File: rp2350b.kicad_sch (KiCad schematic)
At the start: 34 parts, among them J6 SM03B-SRSS-TB, SW1 SW_Push, SW2 SW_Push, U10 W25Q128JVS, U13 RP2350_80QFN, Y2 ABM8-272-T3

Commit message: Break out RP2350
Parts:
- SW1, SW2: footprint Button_Switch_SMD:SW_Push_1P1T_NO_Vertical_Wuerth_434133025816 -> Button_Switch_SMD:SW_Push_1P1T_XKB_TS-1187A; LCSC (none) -> C318884
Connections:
- net +1V1: now also C20.1, C22.1, C23.1, U13.10 (DVDD), U13.32 (DVDD), U13.51 (DVDD)
- net SWCLK: no longer U13.33 (SWCLK)
- net SWD: no longer U13.34 (SWD)
- net GPIO0 renamed GPIO00
- net GPIO1 renamed GPIO01
- net GPIO2 renamed GPIO02
- net GPIO3 renamed GPIO03
- net GPIO4 renamed GPIO04
- net GPIO5 renamed GPIO05
- net GPIO6 renamed GPIO06
- net GPIO7 renamed GPIO07
- net GPIO8 renamed GPIO08
- net GPIO9 renamed GPIO09
- new net SWD.SWCLK: U13.33 (SWCLK)
- new net SWD.SWD: U13.34 (SWD)
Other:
- moved on the sheet: J6

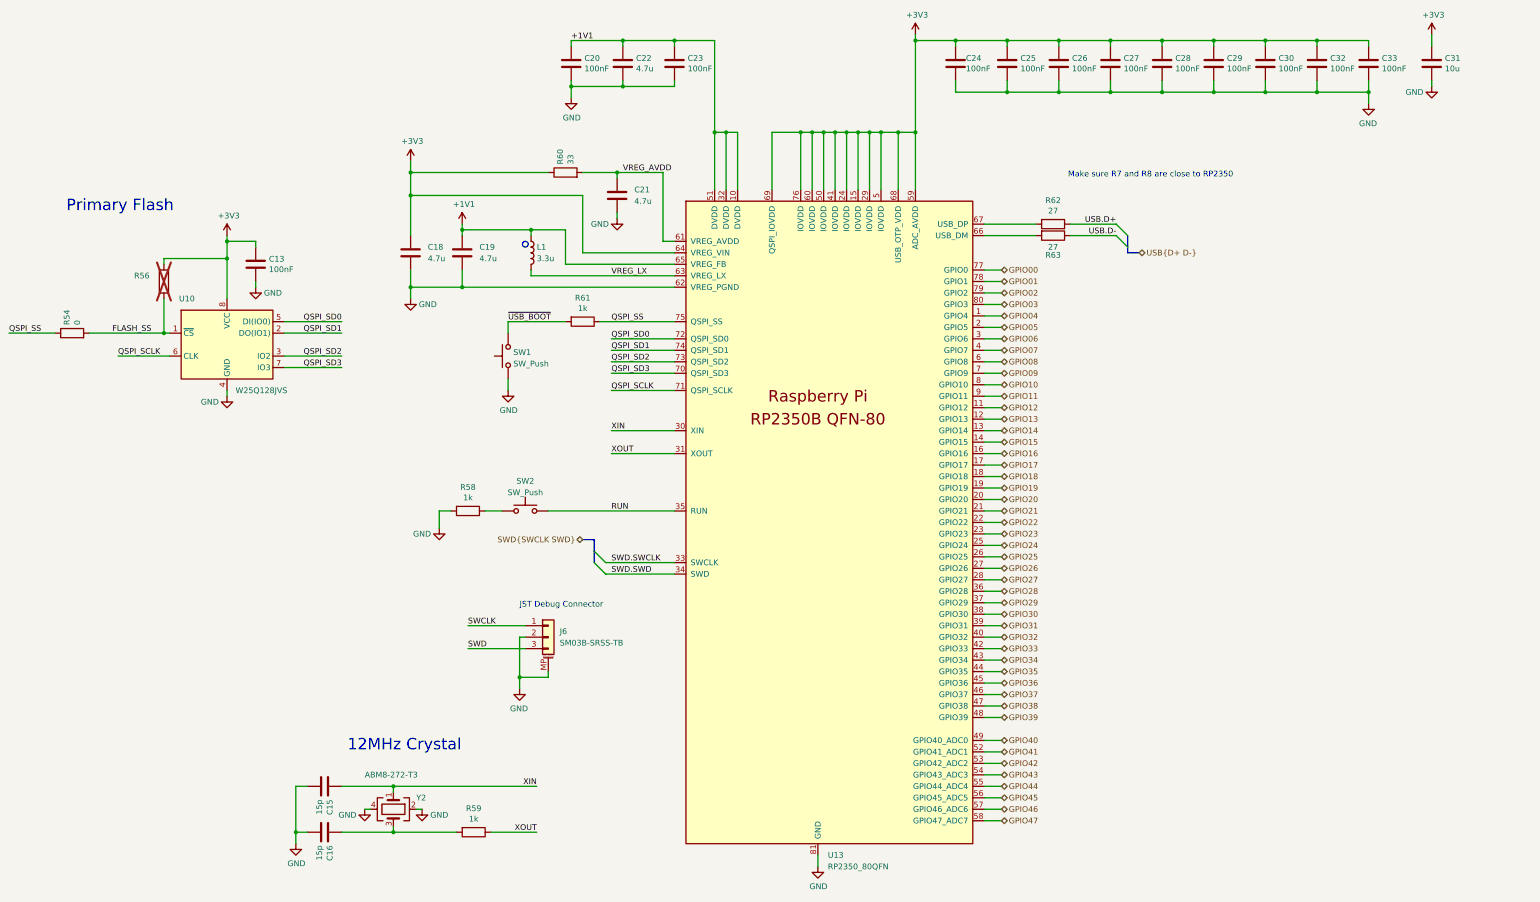
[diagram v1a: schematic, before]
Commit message: Do pin assignment for tester
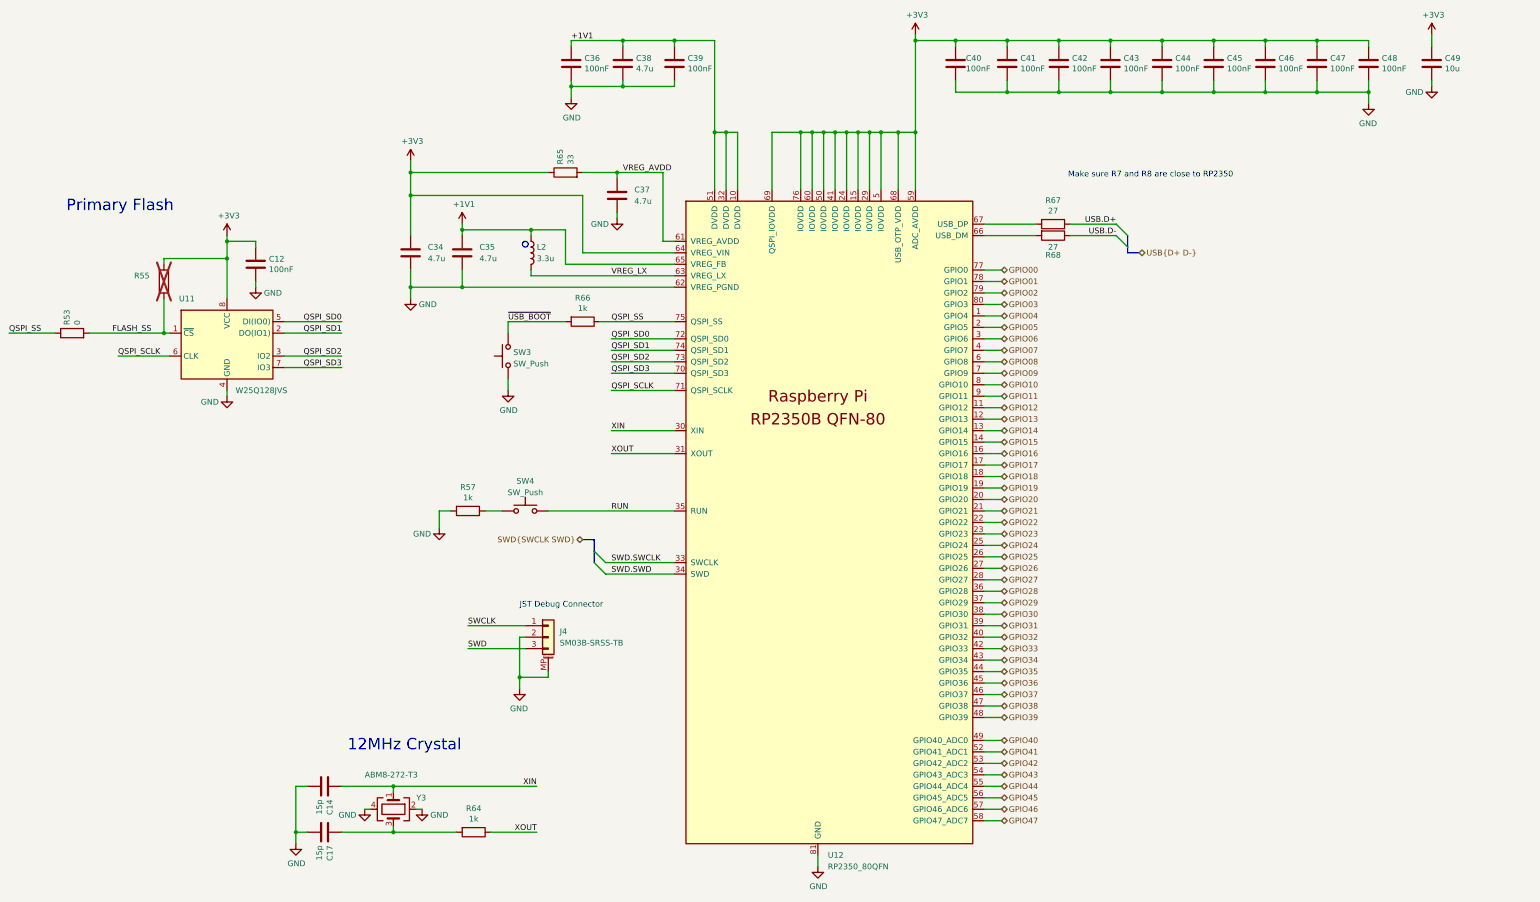
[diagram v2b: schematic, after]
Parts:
- renumbered C13 to C12, C15 to C14, C16 to C17, C18 to C34, C19 to C35, C20 to C36, C21 to C37, C22 to C38, C23 to C39, C24 to C40, C25 to C41, C26 to C42, C27 to C43, C28 to C44, C29 to C45, C30 to C46, C32 to C47, C33 to C48, C31 to C49, J6 to J4, L1 to L2, R54 to R53, R56 to R55, R58 to R57, R59 to R64, R60 to R65, R61 to R66, R62 to R67, R63 to R68, SW1 to SW3, SW2 to SW4, U10 to U11, U13 to U12, Y2 to Y3

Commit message: Start Layout
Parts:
- removed C12: 100nF, Capacitor_SMD:C_0402_1005Metric, symbol Device:C
- removed R53: 0, Resistor_SMD:R_0402_1005Metric, symbol Device:R
- removed R55: DNF, Resistor_SMD:R_0402_1005Metric, symbol Device:R
- removed U11: W25Q128JVS, Package_SO:SOIC-8_5.23x5.23mm_P1.27mm, symbol Memory_Flash:W25Q128JVS
- added C50: 100nF, Capacitor_SMD:C_0402_1005Metric, symbol Device:C
- added U16: W25Q128JVS, Package_SO:SOIC-8_5.3x5.3mm_P1.27mm, symbol Memory_Flash:W25Q128JVS
- J6: renamed from J4; footprint Connector_JST:JST_SH_SM03B-SRSS-TB_1x03-1MP_P1.00mm_Horizontal -> Connector_JST:JST_SH_BM03B-SRSS-TB_1x03-1MP_P1.00mm_Vertical; LCSC (none) -> C160389
- U13: renamed from U12; symbol MCU_RaspberryPi_RP2350:RP2350_80QFN -> Project_Specific:RP2350_80QFN
- renumbered C14 to C15, C17 to C16, C34 to C18, C35 to C19, C36 to C20, C37 to C21, C38 to C22, C39 to C23, C40 to C24, C41 to C25, C42 to C26, C43 to C27, C44 to C28, C45 to C29, C46 to C30, C47 to C31, C48 to C32, C49 to C33, L2 to L1, R57 to R58, R64 to R59, R65 to R60, R66 to R61, R67 to R62, R68 to R63, SW3 to SW1, SW4 to SW2, Y3 to Y2
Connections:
- net SWCLK is gone; now on net SWD.SWCLK: J6.1 (Pin_1)
- net SWD is gone; now on net SWD.SWD: J6.3 (Pin_3)
- net +3V3: now also C50.1, U16.8 (VCC)
- net GND: now also C50.2, U16.4 (GND)
- net QSPI_SCLK: now also U16.6 (CLK)
- net QSPI_SD0: now also U16.5 (DI/IO_{0})
- net QSPI_SD1: now also U16.2 (DO/IO_{1})
- net QSPI_SD2: now also U16.3 (~{WP}/IO_{2})
- net QSPI_SD3: now also U16.7 (~{HOLD}/~{RESET}/IO_{3})
- net QSPI_SS: now also U16.1 (~{CS})
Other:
- note removed: "Primary Flash"

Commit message: WIP
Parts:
- removed C50: 100nF, Capacitor_SMD:C_0402_1005Metric, symbol Device:C
- removed U16: W25Q128JVS, Package_SO:SOIC-8_5.3x5.3mm_P1.27mm, symbol Memory_Flash:W25Q128JVS
- C15, C16: LCSC (none) -> C1548
- C18, C19, C21, C22: LCSC (none) -> C23733
- C33: LCSC (none) -> C15850
- J6: value SM03B-SRSS-TB -> BM03B-SRSS-TB
- R58, R59, R61: value 1k -> 1K; LCSC (none) -> C11702
- R60: LCSC (none) -> C25105
- R62, R63: LCSC (none) -> C138021
- U13: value RP2350_80QFN -> RP2354B; footprint ProjectSpecific:RP2350-QFN-80-1EP_10x10_P0.4mm_EP3.4x3.4mm_ThermalVias -> RP2350_80QFN_minimal:RP2350-QFN-80-1EP_10x10_P0.4mm_EP3.4x3.4mm_ThermalVias; symbol Project_Specific:RP2350_80QFN -> Project_Specific:RP2354B; LCSC (none) -> C39843328
- Y2: LCSC (none) -> C20625731
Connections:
- net QSPI_SCLK: no longer names the net of U13.71 (QSPI_SCLK)
- net QSPI_SD0: no longer names the net of U13.72 (QSPI_SD0)
- net QSPI_SD1: no longer names the net of U13.74 (QSPI_SD1)
- net QSPI_SD2: no longer names the net of U13.73 (QSPI_SD2)
- net QSPI_SD3: no longer names the net of U13.70 (QSPI_SD3)
- no-connect marks 0 -> 5

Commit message: layout finished
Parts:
- U13: footprint RP2350_80QFN_minimal:RP2350-QFN-80-1EP_10x10_P0.4mm_EP3.4x3.4mm_ThermalVias -> Package_DFN_QFN:QFN-80-1EP_10x10mm_P0.4mm_EP3.4x3.4mm_ThermalVias
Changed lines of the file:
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@@
 			)
 		)
-		(property "Footprint" "RP2350_80QFN_minimal:RP2350-QFN-80-1EP_10x10_P0.4mm_EP3.4x3.4mm_ThermalVias"
+		(property "Footprint" "Package_DFN_QFN:QFN-80-1EP_10x10mm_P0.4mm_EP3.4x3.4mm_ThermalVias"
 			(at 179.07 130.81 0)
 			(effects

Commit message: JLC rotations
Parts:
- J6, L1: FT Rotation Offset (none) -> 180
- U13: FT Rotation Offset (none) -> -90
